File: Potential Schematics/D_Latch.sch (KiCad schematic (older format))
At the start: 2 parts, among them U18 74LS04, U7 74LS09

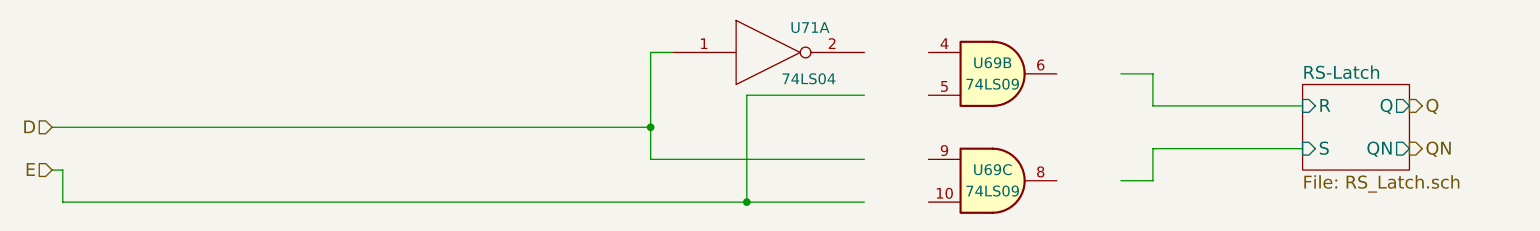
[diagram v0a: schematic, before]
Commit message: Added Registers to Top Schematic
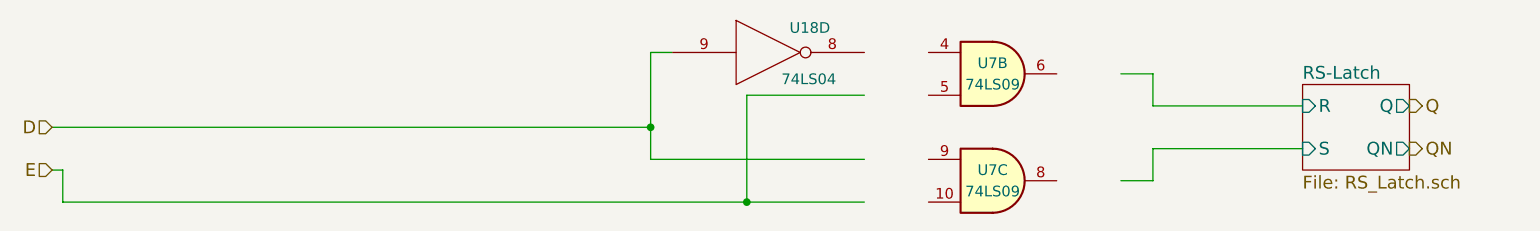
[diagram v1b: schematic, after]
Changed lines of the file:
@@
 $Descr A4 11693 8268
 encoding utf-8
-Sheet 131 449
+Sheet 26 449
 Title "D Latch"
 Date "2018-09-14"
@@
 $Comp
 L 74LS04 U18
-U 1 1 5B9C16FA
+U 4 1 5B9C16FA
 P 4850 3400
 AR Path="/5B9D167A/5B9C0EA0/5B9C0F16/5B9C0F19/5B9C0F1C/5B9C16FA" Ref="U18"  Part="4"
@@
 AR Path="/5B9D167A/5B9C0EA0/5B9DB28B/5B9C41DB/5B9C0F1C/5B9C16FA" Ref="U176"  Part="4"
 AR Path="/5B9D167A/5B9C0EA0/5B9DB28B/5B9C41DB/5B9C312A/5B9C16FA" Ref="U176"  Part="5"
-F 0 "U71" H 5045 3515 50  0000 C CNN
+F 0 "U18" H 5045 3515 50  0000 C CNN
 F 1 "74LS04" H 5040 3275 50  0000 C CNN
 F 2 "" H 4850 3400 50  0001 C CNN
 F 3 "" H 4850 3400 50  0001 C CNN
-	1    4850 3400
+	4    4850 3400
 	1    0    0    -1
 $EndComp
@@
 AR Path="/5B9D167A/5B9C0EA0/5B9DB28B/5B9C41DB/5B9C0F1C/5B9C17F5" Ref="U177"  Part="2"
 AR Path="/5B9D167A/5B9C0EA0/5B9DB28B/5B9C41DB/5B9C312A/5B9C17F5" Ref="U177"  Part="4"
-F 0 "U69" H 5900 3550 50  0000 C CNN
+F 0 "U7" H 5900 3550 50  0000 C CNN
 F 1 "74LS09" H 5900 3450 50  0000 C CNN
 F 2 "" H 5900 3500 50  0001 C CNN
@@
 AR Path="/5B9D167A/5B9C0EA0/5B9DB28B/5B9C41DB/5B9C0F1C/5B9C1BD4" Ref="U177"  Part="3"
 AR Path="/5B9D167A/5B9C0EA0/5B9DB28B/5B9C41DB/5B9C312A/5B9C1BD4" Ref="U179"  Part="1"
-F 0 "U69" H 5900 4050 50  0000 C CNN
+F 0 "U7" H 5900 4050 50  0000 C CNN
 F 1 "74LS09" H 5900 3950 50  0000 C CNN
 F 2 "" H 5900 4000 50  0001 C CNN

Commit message: Adding Multiply Devide
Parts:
- U18: symbol 74LS04 -> 4-bit_processor-rescue:74LS04
- U7: symbol 74LS09 -> 4-bit_processor-rescue:74LS09
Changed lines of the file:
@@
-EESchema Schematic File Version 2
-LIBS:power
-LIBS:device
-LIBS:switches
-LIBS:relays
-LIBS:motors
-LIBS:transistors
-LIBS:conn
-LIBS:linear
-LIBS:regul
-LIBS:74xx
-LIBS:cmos4000
-LIBS:adc-dac
-LIBS:memory
-LIBS:xilinx
-LIBS:microcontrollers
-LIBS:dsp
-LIBS:microchip
-LIBS:analog_switches
-LIBS:motorola
-LIBS:texas
-LIBS:intel
-LIBS:audio
-LIBS:interface
-LIBS:digital-audio
-LIBS:philips
-LIBS:display
-LIBS:cypress
-LIBS:siliconi
-LIBS:opto
-LIBS:atmel
-LIBS:contrib
-LIBS:valves
+EESchema Schematic File Version 4
 LIBS:4-bit_processor-cache
-EELAYER 25 0
+EELAYER 26 0
 EELAYER END
 $Descr A4 11693 8268
 encoding utf-8
-Sheet 26 449
+Sheet 26 451
 Title "D Latch"
 Date "2018-09-14"
@@
 E
 $Comp
-L 74LS04 U18
+L 4-bit_processor-rescue:74LS04 U18
 U 4 1 5B9C16FA
 P 4850 3400
@@
 $EndComp
 $Comp
-L 74LS09 U7
+L 4-bit_processor-rescue:74LS09 U7
 U 2 1 5B9C17F5
 P 5900 3500
@@
 $EndComp
 $Comp
-L 74LS09 U7
+L 4-bit_processor-rescue:74LS09 U7
 U 3 1 5B9C1BD4
 P 5900 4000

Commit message: Finished PCB
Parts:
- U34: renamed from U7; footprint (none) -> Daniel_Kopp:DIP-14_300_ELL
- U35: renamed from U18; footprint (none) -> Daniel_Kopp:DIP-14_300_ELL
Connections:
- wire segments 15 -> 17
